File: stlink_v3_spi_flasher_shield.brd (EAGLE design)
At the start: 39.2 x 49.9 mm, 10 parts, among them CON1 STLINK_V3_HAT_BRIDGE_AND_UART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

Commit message: Signoff enforce test
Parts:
- moved C2 69.2 mm to (30.5, 20.3)
- moved R5 68.5 mm to (22.9, 34.3), turned to 90 degrees
- moved C1 64.3 mm to (30.5, 17.8)
- moved R2 58.2 mm to (25.4, 27.9), turned to 270 degrees
- moved R3 50.8 mm to (21.6, 16.5), turned to 270 degrees
- moved R1 44.9 mm to (19.1, 16.5), turned to 270 degrees
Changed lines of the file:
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@@
 <element name="CON1" library="stlinkv3" package="STLINKV3_HAT_BRIDGE_MINIMAL" value="STLINK_V3_HAT_BRIDGE_AND_UART_MINIMAL" x="3.81" y="25.4"/>
 <element name="SPI_FLASH" library="martonmiklos" package="SO8_LONG" value="SPI_SO8" x="21.59" y="26.67" rot="R90"/>
-<element name="R1" library="rcl" package="R0603" value="" x="-21.59" y="-2.54"/>
-<element name="R2" library="rcl" package="R0603" value="" x="-21.59" y="-6.35"/>
-<element name="R3" library="rcl" package="R0603" value="" x="-21.59" y="-10.16"/>
-<element name="R5" library="rcl" package="R0603" value="" x="-21.59" y="-17.78"/>
-<element name="C1" library="rcl" package="C0603" value="100nF" x="-20.32" y="-21.59"/>
-<element name="C2" library="rcl" package="C0603" value="1uF" x="-20.32" y="-26.67"/>
+<element name="R1" library="rcl" package="R0603" value="" x="19.05" y="16.51" rot="R270"/>
+<element name="R2" library="rcl" package="R0603" value="" x="25.4" y="27.94" rot="R270"/>
+<element name="R3" library="rcl" package="R0603" value="" x="21.59" y="16.51" rot="R270"/>
+<element name="R5" library="rcl" package="R0603" value="" x="22.86" y="34.29" rot="R90"/>
+<element name="C1" library="rcl" package="C0603" value="100nF" x="30.48" y="17.78"/>
+<element name="C2" library="rcl" package="C0603" value="1uF" x="30.48" y="20.32"/>
 </elements>
 <signals>
@@
 <wire x1="22.4" y1="6.365" x2="23.495" y2="24.07" width="0" layer="19" extent="1-1"/>
 <wire x1="3.81" y1="25.4" x2="19.9" y2="35.56" width="0" layer="19" extent="1-1"/>
-<wire x1="-19.47" y1="-21.59" x2="22.4" y2="6.365" width="0" layer="19" extent="1-1"/>
-<wire x1="-19.47" y1="-26.67" x2="-19.47" y2="-21.59" width="0" layer="19" extent="1-1"/>
+<wire x1="31.33" y1="17.78" x2="22.4" y2="6.365" width="0" layer="19" extent="1-1"/>
+<wire x1="31.33" y1="20.32" x2="31.33" y2="17.78" width="0" layer="19" extent="1-1"/>
 </signal>
 <signal name="VCC">
@@
 <contactref element="SPI_FLASH" pad="5"/>
 <contactref element="R2" pad="1"/>
-<wire x1="-22.44" y1="-6.35" x2="23.495" y2="29.27" width="0" layer="19" extent="1-1"/>
+<wire x1="25.4" y1="28.79" x2="23.495" y2="29.27" width="0" layer="19" extent="1-1"/>
 </signal>
 <signal name="SCK_FLASH">
 <contactref element="SPI_FLASH" pad="6"/>
 <contactref element="R5" pad="1"/>
-<wire x1="-22.44" y1="-17.78" x2="22.225" y2="29.27" width="0" layer="19" extent="1-1"/>
+<wire x1="22.86" y1="33.44" x2="22.225" y2="29.27" width="0" layer="19" extent="1-1"/>
 </signal>
 <signal name="!SS_FLASH">
 <contactref element="SPI_FLASH" pad="1"/>
 <contactref element="R1" pad="1"/>
-<wire x1="-22.44" y1="-2.54" x2="19.685" y2="24.07" width="0" layer="19" extent="1-1"/>
+<wire x1="19.05" y1="17.36" x2="19.685" y2="24.07" width="0" layer="19" extent="1-1"/>
 </signal>
 <signal name="N$1">
 <contactref element="R1" pad="2"/>
 <contactref element="CON1" pad="SPI_1"/>
-<wire x1="17.32" y1="6.365" x2="-20.74" y2="-2.54" width="0" layer="19" extent="1-1"/>
+<wire x1="17.32" y1="6.365" x2="19.05" y2="15.66" width="0" layer="19" extent="1-1"/>
 </signal>
 <signal name="N$2">
 <contactref element="R2" pad="2"/>
 <contactref element="CON1" pad="SPI_3"/>
-<wire x1="18.59" y1="6.365" x2="-20.74" y2="-6.35" width="0" layer="19" extent="1-1"/>
+<wire x1="18.59" y1="6.365" x2="25.4" y2="27.09" width="0" layer="19" extent="1-1"/>
 </signal>
 <signal name="N$3">
 <contactref element="R3" pad="2"/>
 <contactref element="CON1" pad="SPI_5"/>
-<wire x1="19.86" y1="6.365" x2="-20.74" y2="-10.16" width="0" layer="19" extent="1-1"/>
+<wire x1="19.86" y1="6.365" x2="21.59" y2="15.66" width="0" layer="19" extent="1-1"/>
 </signal>
 <signal name="N$4">
 <contactref element="R5" pad="2"/>
 <contactref element="CON1" pad="SPI_7"/>
-<wire x1="21.13" y1="6.365" x2="-20.74" y2="-17.78" width="0" layer="19" extent="1-1"/>
+<wire x1="21.13" y1="6.365" x2="22.86" y2="35.14" width="0" layer="19" extent="1-1"/>
 </signal>
 <signal name="MISO_FLASH">
 <contactref element="SPI_FLASH" pad="2"/>
 <contactref element="R3" pad="1"/>
-<wire x1="-22.44" y1="-10.16" x2="20.955" y2="24.07" width="0" layer="19" extent="1-1"/>
+<wire x1="21.59" y1="17.36" x2="20.955" y2="24.07" width="0" layer="19" extent="1-1"/>
 </signal>
 <signal name="+5V">
@@
 <contactref element="C1" pad="1"/>
 <contactref element="C2" pad="1"/>
-<wire x1="-21.17" y1="-21.59" x2="-21.17" y2="-26.67" width="0" layer="19" extent="1-1"/>
-<wire x1="22.4" y1="7.635" x2="-21.17" y2="-21.59" width="0" layer="19" extent="1-1"/>
+<wire x1="29.63" y1="17.78" x2="29.63" y2="20.32" width="0" layer="19" extent="1-1"/>
+<wire x1="22.4" y1="7.635" x2="29.63" y2="17.78" width="0" layer="19" extent="1-1"/>
 </signal>
 </signals>

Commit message: Signoff test #₂
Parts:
- moved C2 2.54 mm to (30.5, 22.9)
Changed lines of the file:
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@@
 <element name="R5" library="rcl" package="R0603" value="" x="22.86" y="34.29" rot="R90"/>
 <element name="C1" library="rcl" package="C0603" value="100nF" x="30.48" y="17.78"/>
-<element name="C2" library="rcl" package="C0603" value="1uF" x="30.48" y="20.32"/>
+<element name="C2" library="rcl" package="C0603" value="1uF" x="30.48" y="22.86"/>
 </elements>
 <signals>
@@
 <wire x1="3.81" y1="25.4" x2="19.9" y2="35.56" width="0" layer="19" extent="1-1"/>
 <wire x1="31.33" y1="17.78" x2="22.4" y2="6.365" width="0" layer="19" extent="1-1"/>
-<wire x1="31.33" y1="20.32" x2="31.33" y2="17.78" width="0" layer="19" extent="1-1"/>
+<wire x1="31.33" y1="22.86" x2="31.33" y2="17.78" width="0" layer="19" extent="1-1"/>
 </signal>
 <signal name="VCC">
@@
 <contactref element="C1" pad="1"/>
 <contactref element="C2" pad="1"/>
-<wire x1="29.63" y1="17.78" x2="29.63" y2="20.32" width="0" layer="19" extent="1-1"/>
+<wire x1="29.63" y1="17.78" x2="29.63" y2="22.86" width="0" layer="19" extent="1-1"/>
 <wire x1="22.4" y1="7.635" x2="29.63" y2="17.78" width="0" layer="19" extent="1-1"/>
 </signal>

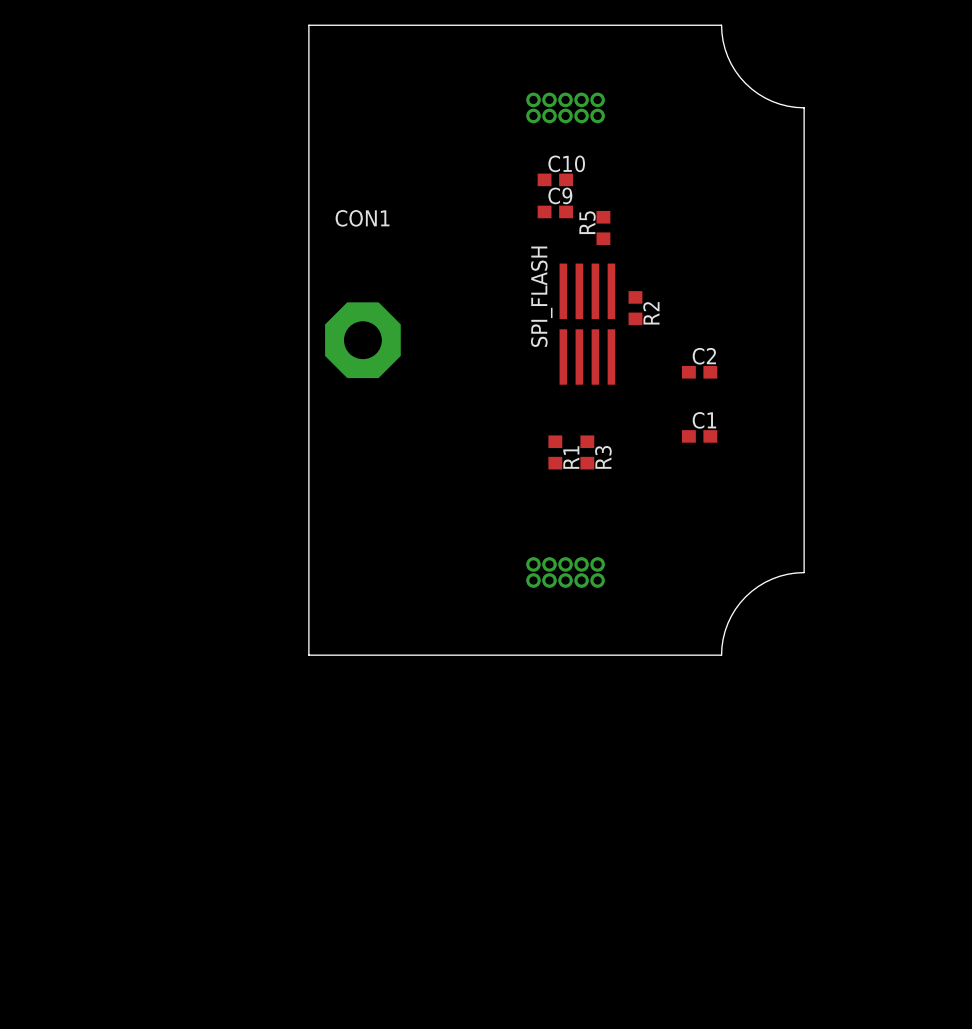
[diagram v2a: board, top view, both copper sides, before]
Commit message: Added SPI socket
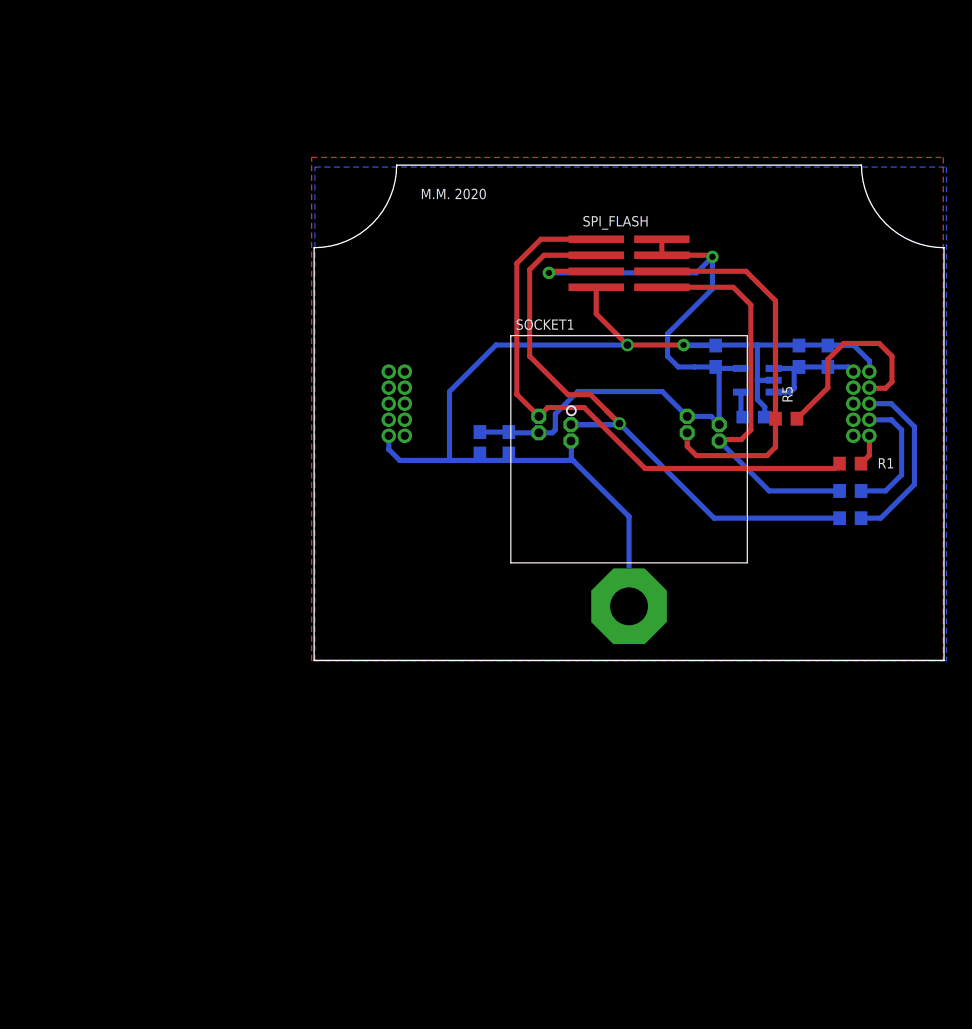
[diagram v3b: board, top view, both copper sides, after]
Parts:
- added C5: 1uF, rcl:C0603
- added C6: 470pF, rcl:C0603
- added SOCKET1: OTS-16-03, OTS_IC_sockets:OTS-16-03
- added U2: MIC5205-3.3YM5-TR, LTC_By_element14_Batch_1:SOT95P280X145-5N
- moved CON1 29.8 mm to (24.9, 4.32), turned to 90 degrees
- moved R1 23.4 mm to (42.4, 15.6), turned to 0 degrees
- moved R2 22.3 mm to (42.4, 13.5), flipped to the bottom, turned to 180 degrees
- moved R3 21.5 mm to (42.4, 11.3), flipped to the bottom, turned to 180 degrees
- moved C10 21.2 mm to (15.4, 17.3), flipped to the bottom, turned to 270 degrees
- moved R5 20.9 mm to (37.3, 19.2), turned to 0 degrees
- moved C9 19.2 mm to (13.1, 17.3), flipped to the bottom, turned to 270 degrees
- moved C1 12.0 mm to (40.6, 24.1), flipped to the bottom, turned to 90 degrees
- moved C2 7.98 mm to (38.4, 24.1), flipped to the bottom, turned to 90 degrees
- moved SPI_FLASH 5.85 mm to (24.9, 31.5), turned to 0 degrees
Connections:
- net N$1 renamed !SS_STLINK
- net N$2 renamed MOSI_STLINK
- net N$3 renamed MISO_STLINK
- net N$4 renamed SCK_STLINK
- removed net VCC: C10.1, C9.1, SPI_FLASH.3, SPI_FLASH.7, SPI_FLASH.8
- new net +3V3: C10.1, C5.1, C9.1, SOCKET1.3, SOCKET1.7, SOCKET1.8, SPI_FLASH.3, SPI_FLASH.7, SPI_FLASH.8, U2.5
- new net N$5: C6.1, U2.4
- net !SS_FLASH: now also SOCKET1.1
- net +5V: now also U2.1, U2.3
- net GND: now also C5.2, C6.2, SOCKET1.4, U2.2
- net MISO_FLASH: now also SOCKET1.2
- net MOSI_FLASH: now also SOCKET1.5
- net SCK_FLASH: now also SOCKET1.6
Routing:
- net GND: track 0.00 -> 91.1 mm, vias 0 -> 2
- net +3V3: track 0.00 -> 64.9 mm, vias 0 -> 2
- net MISO_FLASH: track 0.00 -> 51.6 mm, vias 0 -> 1
- net !SS_FLASH: track 0.00 -> 46.2 mm
- net MOSI_FLASH: track 0.00 -> 31.6 mm
- net SCK_FLASH: track 0.00 -> 30.2 mm
- net SCK_STLINK: track 0.00 -> 15.8 mm
- net MISO_STLINK: track 0.00 -> 14.2 mm
- net MOSI_STLINK: track 0.00 -> 10.2 mm
- net +5V: track 0.00 -> 9.94 mm
- net !SS_STLINK: track 0.00 -> 2.48 mm
- net N$5: track 0.00 -> 2.06 mm
- added copper zone on layer 1, net GND
- added copper zone on layer 16, net GND
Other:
- board size 39.2 x 49.9 mm -> 49.9 x 39.2 mm
- board text added: "M.M. 2020"

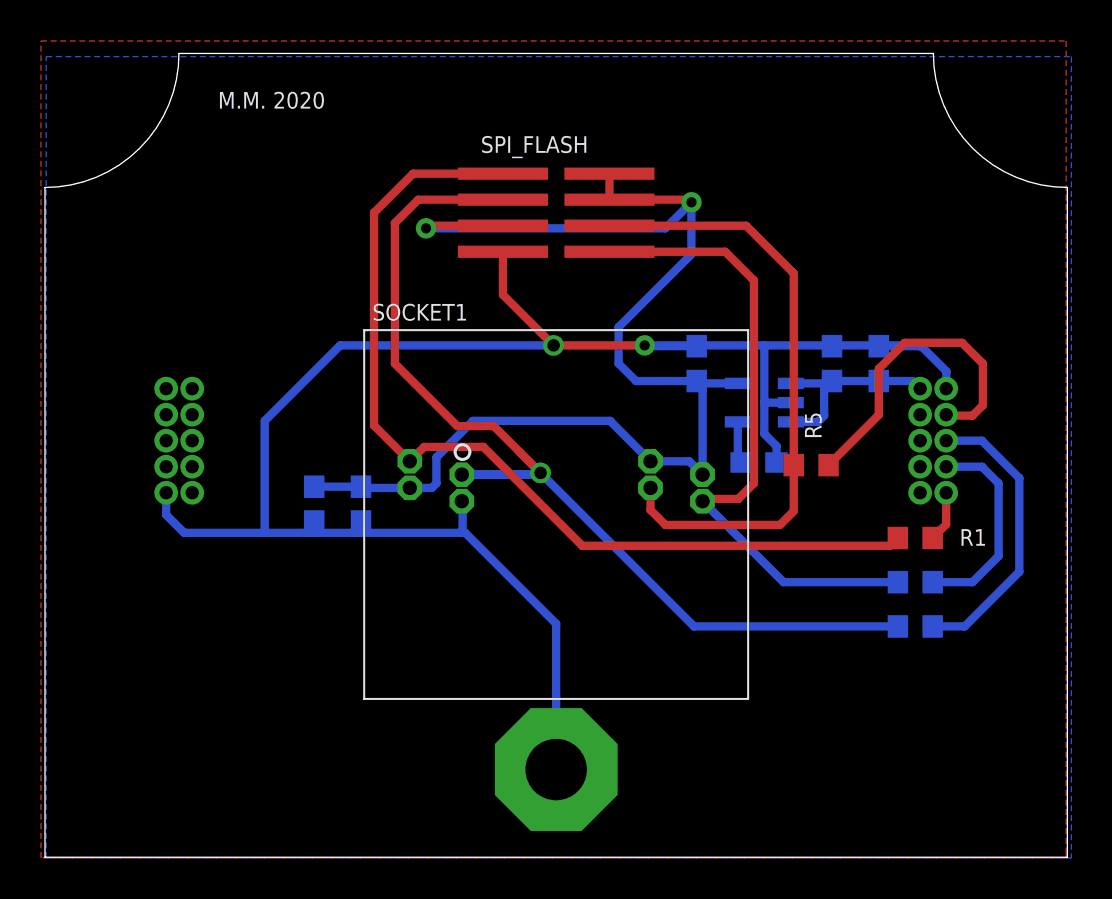
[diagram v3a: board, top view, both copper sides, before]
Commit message: - Added SOP16 SPI footprint - Fixup OTS socket footprint
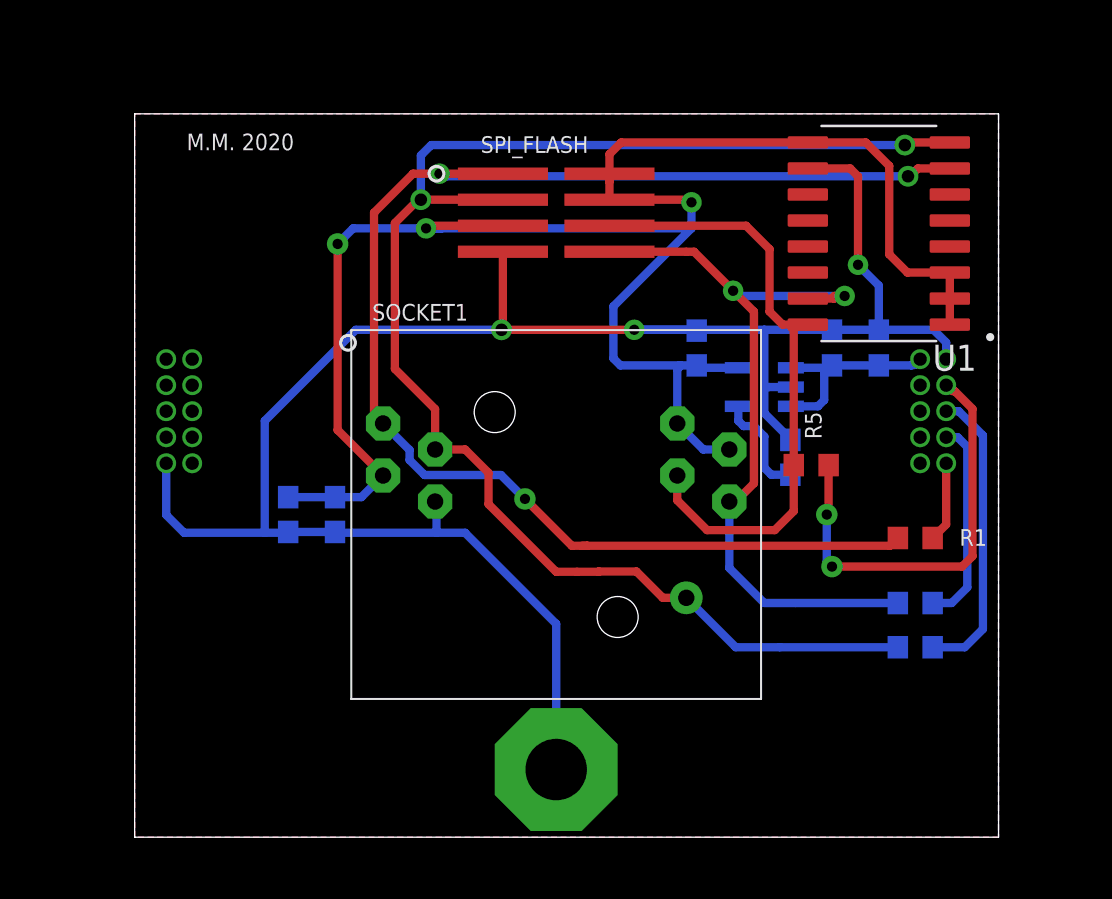
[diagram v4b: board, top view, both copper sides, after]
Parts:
- added U1: MX25L25635E, SparkFun:SOP127P780X200-16N
- CON1: value STLINK_V3_HAT_BRIDGE_AND_UART_MINIMAL -> STLINK_V3_HAT_BRIDGE_AND_UART_MINIMALCONTOURLESS; device stlinkv3:STLINKV3_HAT_BRIDGE_MINIMAL -> stlinkv3:STLINKV3_HAT_BRIDGE_MINIMAL_CONTOURLESS
- R1, R2, R3, R5: value (none) -> 51
- moved C6 1.55 mm to (36.3, 19.6), turned to 90 degrees
- moved C10 1.37 mm to (14.1, 16.8)
- moved C9 1.37 mm to (11.8, 16.8)
- moved R2 1.02 mm to (42.4, 12.4)
- moved R3 1.02 mm to (42.4, 10.3)
- moved C1 0.76 mm to (40.6, 24.9)
- moved C2 0.76 mm to (38.4, 24.9)
- moved C5 0.76 mm to (31.8, 24.9)
- moved U2 0.76 mm to (35.1, 23.0)
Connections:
- net !SS_FLASH: now also U1.7
- net +3V3: now also U1.1, U1.2, U1.3, U1.9
- net GND: now also U1.10
- net MISO_FLASH: now also U1.8
- net MOSI_FLASH: now also U1.15
- net SCK_FLASH: now also U1.16
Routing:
- net +3V3: track 64.9 -> 92.4 mm, vias 2 -> 3
- net !SS_FLASH: track 46.2 -> 71.5 mm, vias 0 -> 3
- net MISO_FLASH: track 51.6 -> 73.3 mm, vias 1 -> 3
- net GND: track 91.1 -> 99.2 mm, vias 2 -> 3
- net MOSI_FLASH: track 31.6 -> 37.9 mm, vias 0 -> 2
- net SCK_STLINK: track 15.8 -> 21.1 mm, vias 0 -> 2
- net N$5: track 2.06 -> 5.24 mm
- net !SS_STLINK: track 2.48 -> 3.92 mm
- net SCK_FLASH: track 30.2 -> 31.2 mm
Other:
- board size 49.9 x 39.2 mm -> 42.2 x 35.3 mm
